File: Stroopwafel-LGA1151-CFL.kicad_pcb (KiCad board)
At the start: 2 copper layers, 1 part

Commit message: rotated socket
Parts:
- turned JCPU1 to 180 degrees
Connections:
- JCPU1 pad AB40: (no net) -> unconnected-(JCPU1B-DDR_VREF_CA-PadAB40)
- JCPU1 pad AC39: (no net) -> unconnected-(JCPU1B-DDR1_VREF_DQ-PadAC39)
- JCPU1 pad AC40: (no net) -> unconnected-(JCPU1B-DDR0_VREF_DQ-PadAC40)
- JCPU1 pad AD34: (no net) -> unconnected-(JCPU1B-DDR1_DQ_0/DDR0_DQ_16-PadAD34)
- JCPU1 pad AD35: (no net) -> unconnected-(JCPU1B-DDR1_DQ_1/DDR0_DQ_17-PadAD35)
- JCPU1 pad AE34: (no net) -> unconnected-(JCPU1B-DDR1_DQ_5/DDR0_DQ_21-PadAE34)
- JCPU1 pad AE35: (no net) -> unconnected-(JCPU1B-DDR1_DQ_4/DDR0_DQ_20-PadAE35)
- JCPU1 pad AE6: (no net) -> unconnected-(JCPU1B-DDR1_DQ_58/DDR1_DQ_58-PadAE6)
- JCPU1 pad AE7: (no net) -> unconnected-(JCPU1B-DDR1_DQ_62/DDR1_DQ_62-PadAE7)
- JCPU1 pad AF34: (no net) -> unconnected-(JCPU1B-DDR1_DQSN_0/DDR0_DQSN_2-PadAF34)
- JCPU1 pad AF35: (no net) -> unconnected-(JCPU1B-DDR1_DQSP_0/DDR0_DQSP_2-PadAF35)
- JCPU1 pad AF38: (no net) -> unconnected-(JCPU1A-DDR0_DQSP_0/DDR0_DQSP_0-PadAF38)
- JCPU1 pad AF39: (no net) -> unconnected-(JCPU1A-DDR0_DQSN_0/DDR0_DQSN_0-PadAF39)
- JCPU1 pad AF6: (no net) -> unconnected-(JCPU1B-DDR1_DQ_63/DDR1_DQ_63-PadAF6)
- JCPU1 pad AF7: (no net) -> unconnected-(JCPU1B-DDR1_DQ_59/DDR1_DQ_59-PadAF7)
- JCPU1 pad AG34: (no net) -> unconnected-(JCPU1B-DDR1_DQ_6/DDR0_DQ_22-PadAG34)
- JCPU1 pad AG35: (no net) -> unconnected-(JCPU1B-DDR1_DQ_2/DDR0_DQ_18-PadAG35)
- JCPU1 pad AG6: (no net) -> unconnected-(JCPU1B-DDR1_DQSN_7/DDR1_DQSN_7-PadAG6)
- JCPU1 pad AG7: (no net) -> unconnected-(JCPU1B-DDR1_DQSP_7/DDR1_DQSP_7-PadAG7)
- JCPU1 pad AH34: (no net) -> unconnected-(JCPU1B-DDR1_DQ_7/DDR0_DQ_23-PadAH34)
- JCPU1 pad AH35: (no net) -> unconnected-(JCPU1B-DDR1_DQ_3/DDR0_DQ_19-PadAH35)
- JCPU1 pad AH6: (no net) -> unconnected-(JCPU1B-DDR1_DQ_61/DDR1_DQ_61-PadAH6)
- JCPU1 pad AH7: (no net) -> unconnected-(JCPU1B-DDR1_DQ_60/DDR1_DQ_60-PadAH7)
- JCPU1 pad AJ2: (no net) -> unconnected-(JCPU1A-DDR0_DQSP_7/DDR1_DQSP_5-PadAJ2)
- JCPU1 pad AJ3: (no net) -> unconnected-(JCPU1A-DDR0_DQSN_7/DDR1_DQSN_5-PadAJ3)
- JCPU1 pad AJ6: (no net) -> unconnected-(JCPU1B-DDR1_DQ_56/DDR1_DQ_56-PadAJ6)
- JCPU1 pad AJ7: (no net) -> unconnected-(JCPU1B-DDR1_DQ_57/DDR1_DQ_57-PadAJ7)
- JCPU1 pad AK31: (no net) -> unconnected-(JCPU1B-DDR1_DQ_14/DDR0_DQ_30-PadAK31)
- JCPU1 pad AK32: (no net) -> unconnected-(JCPU1B-DDR1_DQ_10/DDR0_DQ_26-PadAK32)
- JCPU1 pad AK33: (no net) -> unconnected-(JCPU1B-DDR1_DQSN_1/DDR0_DQSN_3-PadAK33)
- JCPU1 pad AK34: (no net) -> unconnected-(JCPU1B-DDR1_DQ_12/DDR0_DQ_28-PadAK34)
- JCPU1 pad AK35: (no net) -> unconnected-(JCPU1B-DDR1_DQ_8/DDR0_DQ_24-PadAK35)
- JCPU1 pad AK38: (no net) -> unconnected-(JCPU1A-DDR0_DQSP_1/DDR0_DQSP_1-PadAK38)
- JCPU1 pad AK39: (no net) -> unconnected-(JCPU1A-DDR0_DQSN_1/DDR0_DQSN_1-PadAK39)
- JCPU1 pad AL10: (no net) -> unconnected-(JCPU1B-DDR1_DQ_49/DDR1_DQ_49-PadAL10)
- JCPU1 pad AL12: (no net) -> unconnected-(JCPU1B-DDR1_DQ_39/DDR1_DQ_23-PadAL12)
- JCPU1 pad AL13: (no net) -> unconnected-(JCPU1B-DDR1_DQ_35/DDR1_DQ_19-PadAL13)
- JCPU1 pad AL15: (no net) -> unconnected-(JCPU1B-DDR1_ODT_3-PadAL15)
- JCPU1 pad AL16: (no net) -> unconnected-(JCPU1B-DDR1_ODT_1-PadAL16)
- JCPU1 pad AL17: (no net) -> unconnected-(JCPU1B-DDR1_MA_14-PadAL17)
- JCPU1 pad AL18: (no net) -> unconnected-(JCPU1B-DDR1_BA_0-PadAL18)
- JCPU1 pad AL19: (no net) -> unconnected-(JCPU1B-DDR1_MA_0-PadAL19)
- JCPU1 pad AL20: (no net) -> unconnected-(JCPU1B-DDR1_PAR-PadAL20)
- JCPU1 pad AL22: (no net) -> unconnected-(JCPU1B-DDR1_MA_1-PadAL22)
- JCPU1 pad AL23: (no net) -> unconnected-(JCPU1B-DDR1_MA_5-PadAL23)
- JCPU1 pad AL25: (no net) -> unconnected-(JCPU1B-DDR1_ECC_6-PadAL25)
- JCPU1 pad AL26: (no net) -> unconnected-(JCPU1B-DDR1_ECC_7-PadAL26)
- JCPU1 pad AL28: (no net) -> unconnected-(JCPU1B-DDR1_DQ_29/DDR0_DQ_61-PadAL28)
- JCPU1 pad AL29: (no net) -> unconnected-(JCPU1B-DDR1_DQ_24/DDR0_DQ_56-PadAL29)
- JCPU1 pad AL31: (no net) -> unconnected-(JCPU1B-DDR1_DQ_15/DDR0_DQ_31-PadAL31)
- JCPU1 pad AL32: (no net) -> unconnected-(JCPU1B-DDR1_DQ_11/DDR0_DQ_27-PadAL32)
- JCPU1 pad AL33: (no net) -> unconnected-(JCPU1B-DDR1_DQSP_1/DDR0_DQSP_3-PadAL33)
- JCPU1 pad AL34: (no net) -> unconnected-(JCPU1B-DDR1_DQ_13/DDR0_DQ_29-PadAL34)
- JCPU1 pad AL35: (no net) -> unconnected-(JCPU1B-DDR1_DQ_9/DDR0_DQ_25-PadAL35)
- JCPU1 pad AL6: (no net) -> unconnected-(JCPU1B-DDR1_DQ_55/DDR1_DQ_55-PadAL6)
- JCPU1 pad AL7: (no net) -> unconnected-(JCPU1B-DDR1_DQ_51/DDR1_DQ_51-PadAL7)
- JCPU1 pad AL8: (no net) -> unconnected-(JCPU1B-DDR1_DQSP_6/DDR1_DQSP_6-PadAL8)
- JCPU1 pad AL9: (no net) -> unconnected-(JCPU1B-DDR1_DQ_53/DDR1_DQ_53-PadAL9)
- JCPU1 pad AM10: (no net) -> unconnected-(JCPU1B-DDR1_DQ_48/DDR1_DQ_48-PadAM10)
- JCPU1 pad AM12: (no net) -> unconnected-(JCPU1B-DDR1_DQ_38/DDR1_DQ_22-PadAM12)
- JCPU1 pad AM13: (no net) -> unconnected-(JCPU1B-DDR1_DQ_34/DDR1_DQ_18-PadAM13)
- JCPU1 pad AM15: (no net) -> unconnected-(JCPU1B-DDR1_CS#_3-PadAM15)
- JCPU1 pad AM16: (no net) -> unconnected-(JCPU1B-DDR1_ODT_0-PadAM16)
- JCPU1 pad AM18: (no net) -> unconnected-(JCPU1B-DDR1_BA_1-PadAM18)
- JCPU1 pad AM20: (no net) -> unconnected-(JCPU1B-DDR1_CKP_0-PadAM20)
- JCPU1 pad AM21: (no net) -> unconnected-(JCPU1B-DDR1_CKN_0-PadAM21)
- JCPU1 pad AM22: (no net) -> unconnected-(JCPU1B-DDR1_MA_2-PadAM22)
- JCPU1 pad AM23: (no net) -> unconnected-(JCPU1B-DDR1_MA_3-PadAM23)
- JCPU1 pad AM25: (no net) -> unconnected-(JCPU1B-DDR1_ECC_3-PadAM25)
- JCPU1 pad AM26: (no net) -> unconnected-(JCPU1B-DDR1_ECC_2-PadAM26)
- JCPU1 pad AM28: (no net) -> unconnected-(JCPU1B-DDR1_DQ_28/DDR0_DQ_60-PadAM28)
- JCPU1 pad AM29: (no net) -> unconnected-(JCPU1B-DDR1_DQ_25/DDR0_DQ_57-PadAM29)
- JCPU1 pad AM6: (no net) -> unconnected-(JCPU1B-DDR1_DQ_54/DDR1_DQ_54-PadAM6)
- JCPU1 pad AM7: (no net) -> unconnected-(JCPU1B-DDR1_DQ_50/DDR1_DQ_50-PadAM7)
- JCPU1 pad AM8: (no net) -> unconnected-(JCPU1B-DDR1_DQSN_6/DDR1_DQSN_6-PadAM8)
- JCPU1 pad AM9: (no net) -> unconnected-(JCPU1B-DDR1_DQ_52/DDR1_DQ_52-PadAM9)
- JCPU1 pad AN12: (no net) -> unconnected-(JCPU1B-DDR1_DQSP_4/DDR1_DQSP_2-PadAN12)
- JCPU1 pad AN13: (no net) -> unconnected-(JCPU1B-DDR1_DQSN_4/DDR1_DQSN_2-PadAN13)
- JCPU1 pad AN15: (no net) -> unconnected-(JCPU1B-DDR1_CS#_1-PadAN15)
- JCPU1 pad AN17: (no net) -> unconnected-(JCPU1B-DDR1_CS#_2-PadAN17)
- JCPU1 pad AN18: (no net) -> unconnected-(JCPU1B-DDR1_MA_16-PadAN18)
- JCPU1 pad AN2: (no net) -> unconnected-(JCPU1A-DDR0_DQSP_6/DDR1_DQSP_4-PadAN2)
- JCPU1 pad AN20: (no net) -> unconnected-(JCPU1B-DDR1_CKP_2-PadAN20)
- JCPU1 pad AN21: (no net) -> unconnected-(JCPU1B-DDR1_CKN_2-PadAN21)
- JCPU1 pad AN25: (no net) -> unconnected-(JCPU1B-DDR1_DQSP_8/DDR1_DQSP_8-PadAN25)
- JCPU1 pad AN26: (no net) -> unconnected-(JCPU1B-DDR1_DQSN_8/DDR1_DQSN_8-PadAN26)
- JCPU1 pad AN28: (no net) -> unconnected-(JCPU1B-DDR1_DQSP_3/DDR0_DQSP_7-PadAN28)
- JCPU1 pad AN29: (no net) -> unconnected-(JCPU1B-DDR1_DQSN_3/DDR0_DQSN_7-PadAN29)
- JCPU1 pad AN3: (no net) -> unconnected-(JCPU1A-DDR0_DQSN_6/DDR1_DQSN_4-PadAN3)
- JCPU1 pad AN31: (no net) -> unconnected-(JCPU1B-DDR1_DQ_22/DDR0_DQ_54-PadAN31)
- JCPU1 pad AN32: (no net) -> unconnected-(JCPU1B-DDR1_DQ_18/DDR0_DQ_50-PadAN32)
- JCPU1 pad AN33: (no net) -> unconnected-(JCPU1B-DDR1_DQSN_2/DDR0_DQSN_6-PadAN33)
- JCPU1 pad AN34: (no net) -> unconnected-(JCPU1B-DDR1_DQ_20/DDR0_DQ_52-PadAN34)
- JCPU1 pad AN35: (no net) -> unconnected-(JCPU1B-DDR1_DQ_17/DDR0_DQ_49-PadAN35)
- JCPU1 pad AP10: (no net) -> unconnected-(JCPU1B-DDR1_DQ_40/DDR1_DQ_24-PadAP10)
- JCPU1 pad AP12: (no net) -> unconnected-(JCPU1B-DDR1_DQ_33/DDR1_DQ_17-PadAP12)
- JCPU1 pad AP13: (no net) -> unconnected-(JCPU1B-DDR1_DQ_37/DDR1_DQ_21-PadAP13)
- JCPU1 pad AP15: (no net) -> unconnected-(JCPU1B-DDR1_ODT_2-PadAP15)
- JCPU1 pad AP16: (no net) -> unconnected-(JCPU1B-DDR1_MA_15-PadAP16)
- JCPU1 pad AP17: (no net) -> unconnected-(JCPU1B-DDR1_CS#_0-PadAP17)
- JCPU1 pad AP18: (no net) -> unconnected-(JCPU1B-DDR1_MA_10-PadAP18)
- JCPU1 pad AP19: (no net) -> unconnected-(JCPU1B-DDR1_CKP_3-PadAP19)
- JCPU1 pad AP20: (no net) -> unconnected-(JCPU1B-DDR1_CKN_3-PadAP20)
- JCPU1 pad AP21: (no net) -> unconnected-(JCPU1B-DDR1_CKN_1-PadAP21)
- JCPU1 pad AP22: (no net) -> unconnected-(JCPU1B-DDR1_CKP_1-PadAP22)
- JCPU1 pad AP23: (no net) -> unconnected-(JCPU1B-DDR1_MA_4-PadAP23)
- JCPU1 pad AP25: (no net) -> unconnected-(JCPU1B-DDR1_ECC_5-PadAP25)
- JCPU1 pad AP26: (no net) -> unconnected-(JCPU1B-DDR1_ECC_4-PadAP26)
- JCPU1 pad AP28: (no net) -> unconnected-(JCPU1B-DDR1_DQ_31/DDR0_DQ_63-PadAP28)
- JCPU1 pad AP29: (no net) -> unconnected-(JCPU1B-DDR1_DQ_26/DDR0_DQ_58-PadAP29)
- JCPU1 pad AP31: (no net) -> unconnected-(JCPU1B-DDR1_DQ_23/DDR0_DQ_55-PadAP31)
- JCPU1 pad AP32: (no net) -> unconnected-(JCPU1B-DDR1_DQ_19/DDR0_DQ_51-PadAP32)
- JCPU1 pad AP33: (no net) -> unconnected-(JCPU1B-DDR1_DQSP_2/DDR0_DQSP_6-PadAP33)
- JCPU1 pad AP34: (no net) -> unconnected-(JCPU1B-DDR1_DQ_21/DDR0_DQ_53-PadAP34)
- JCPU1 pad AP35: (no net) -> unconnected-(JCPU1B-DDR1_DQ_16/DDR0_DQ_48-PadAP35)
- JCPU1 pad AP38: (no net) -> unconnected-(JCPU1A-DDR0_DQSP_2/DDR0_DQSP_4-PadAP38)
- JCPU1 pad AP39: (no net) -> unconnected-(JCPU1A-DDR0_DQSN_2/DDR0_DQSN_4-PadAP39)
- JCPU1 pad AP6: (no net) -> unconnected-(JCPU1B-DDR1_DQ_47/DDR1_DQ_31-PadAP6)
- JCPU1 pad AP7: (no net) -> unconnected-(JCPU1B-DDR1_DQ_43/DDR1_DQ_27-PadAP7)
- JCPU1 pad AP8: (no net) -> unconnected-(JCPU1B-DDR1_DQSP_5/DDR1_DQSP_3-PadAP8)
- JCPU1 pad AP9: (no net) -> unconnected-(JCPU1B-DDR1_DQ_45/DDR1_DQ_29-PadAP9)
- JCPU1 pad AR10: (no net) -> unconnected-(JCPU1B-DDR1_DQ_41/DDR1_DQ_25-PadAR10)
- JCPU1 pad AR12: (no net) -> unconnected-(JCPU1B-DDR1_DQ_32/DDR1_DQ_16-PadAR12)
- JCPU1 pad AR13: (no net) -> unconnected-(JCPU1B-DDR1_DQ_36/DDR1_DQ_20-PadAR13)
- JCPU1 pad AR15: (no net) -> unconnected-(JCPU1B-DDR1_MA_13-PadAR15)
- JCPU1 pad AR25: (no net) -> unconnected-(JCPU1B-DDR1_ECC_0-PadAR25)
- JCPU1 pad AR26: (no net) -> unconnected-(JCPU1B-DDR1_ECC_1-PadAR26)
- JCPU1 pad AR28: (no net) -> unconnected-(JCPU1B-DDR1_DQ_30/DDR0_DQ_62-PadAR28)
- JCPU1 pad AR29: (no net) -> unconnected-(JCPU1B-DDR1_DQ_27/DDR0_DQ_59-PadAR29)
- JCPU1 pad AR6: (no net) -> unconnected-(JCPU1B-DDR1_DQ_46/DDR1_DQ_30-PadAR6)
- JCPU1 pad AR7: (no net) -> unconnected-(JCPU1B-DDR1_DQ_42/DDR1_DQ_26-PadAR7)
- JCPU1 pad AR8: (no net) -> unconnected-(JCPU1B-DDR1_DQSN_5/DDR1_DQSN_3-PadAR8)
- JCPU1 pad AR9: (no net) -> unconnected-(JCPU1B-DDR1_DQ_44/DDR1_DQ_28-PadAR9)
- JCPU1 pad AT16: (no net) -> unconnected-(JCPU1A-DDR0_CKP_3-PadAT16)
- JCPU1 pad AT19: (no net) -> unconnected-(JCPU1A-DDR0_MA_4-PadAT19)
- JCPU1 pad AT20: (no net) -> unconnected-(JCPU1A-DDR0_MA_8-PadAT20)
- JCPU1 pad AT22: (no net) -> unconnected-(JCPU1A-DDR0_MA_9-PadAT22)
- JCPU1 pad AT23: (no net) -> unconnected-(JCPU1A-DDR0_ALERT#-PadAT23)
- JCPU1 pad AU11: (no net) -> unconnected-(JCPU1A-DDR0_CS#_1-PadAU11)
- JCPU1 pad AU12: (no net) -> unconnected-(JCPU1A-DDR0_ODT_2-PadAU12)
- JCPU1 pad AU14: (no net) -> unconnected-(JCPU1A-DDR0_ODT_1-PadAU14)
- JCPU1 pad AU16: (no net) -> unconnected-(JCPU1A-DDR0_CKN_3-PadAU16)
- JCPU1 pad AU17: (no net) -> unconnected-(JCPU1A-DDR0_MA_2-PadAU17)
- JCPU1 pad AU18: (no net) -> unconnected-(JCPU1A-DDR0_MA_1-PadAU18)
- JCPU1 pad AU2: (no net) -> unconnected-(JCPU1A-DDR0_DQSP_5/DDR1_DQSP_1-PadAU2)
- JCPU1 pad AU20: (no net) -> unconnected-(JCPU1A-DDR0_MA_5-PadAU20)
- JCPU1 pad AU21: (no net) -> unconnected-(JCPU1A-DDR0_MA_7-PadAU21)
- JCPU1 pad AU22: (no net) -> unconnected-(JCPU1A-DDR0_MA_11-PadAU22)
- JCPU1 pad AU24: (no net) -> unconnected-(JCPU1A-DDR0_ACT#-PadAU24)
- JCPU1 pad AU26: (no net) -> unconnected-(JCPU1B-DDR1_MA_8-PadAU26)
- JCPU1 pad AU27: (no net) -> unconnected-(JCPU1B-DDR1_MA_11-PadAU27)
- JCPU1 pad AU28: (no net) -> unconnected-(JCPU1B-DDR1_ACT#-PadAU28)
- JCPU1 pad AU29: (no net) -> unconnected-(JCPU1B-DDR1_CKE_3-PadAU29)
- JCPU1 pad AU3: (no net) -> unconnected-(JCPU1A-DDR0_DQSN_5/DDR1_DQSN_1-PadAU3)
- JCPU1 pad AU32: (no net) -> unconnected-(JCPU1A-DDR0_DQSN_8/DDR0_DQSN_8-PadAU32)
- JCPU1 pad AU36: (no net) -> unconnected-(JCPU1A-DDR0_DQSN_3/DDR0_DQSN_5-PadAU36)
- JCPU1 pad AV10: (no net) -> unconnected-(JCPU1A-DDR0_CS#_3-PadAV10)
- JCPU1 pad AV12: (no net) -> unconnected-(JCPU1A-DDR0_MA_13-PadAV12)
- JCPU1 pad AV13: (no net) -> unconnected-(JCPU1A-DDR0_CS#_2-PadAV13)
- JCPU1 pad AV14: (no net) -> unconnected-(JCPU1A-DDR0_MA_14-PadAV14)
- JCPU1 pad AV15: (no net) -> unconnected-(JCPU1A-DDR0_BA_1-PadAV15)
- JCPU1 pad AV16: (no net) -> unconnected-(JCPU1A-DDR0_CKN_2-PadAV16)
- JCPU1 pad AV18: (no net) -> unconnected-(JCPU1A-DDR0_CKN_0-PadAV18)
- JCPU1 pad AV19: (no net) -> unconnected-(JCPU1A-DDR0_MA_3-PadAV19)
- JCPU1 pad AV20: (no net) -> unconnected-(JCPU1A-DDR0_MA_6-PadAV20)
- JCPU1 pad AV22: (no net) -> unconnected-(JCPU1A-DDR0_MA_12-PadAV22)
- JCPU1 pad AV23: (no net) -> unconnected-(JCPU1A-DDR0_BG_1-PadAV23)
- JCPU1 pad AV24: (no net) -> unconnected-(JCPU1A-DDR0_CKE_2-PadAV24)
- JCPU1 pad AV25: (no net) -> unconnected-(JCPU1A-DDR0_CKE_3-PadAV25)
- JCPU1 pad AV27: (no net) -> unconnected-(JCPU1B-DDR1_MA_12-PadAV27)
- JCPU1 pad AV29: (no net) -> unconnected-(JCPU1B-DDR1_CKE_1-PadAV29)
- JCPU1 pad AV32: (no net) -> unconnected-(JCPU1A-DDR0_DQSP_8/DDR0_DQSP_8-PadAV32)
- JCPU1 pad AV36: (no net) -> unconnected-(JCPU1A-DDR0_DQSP_3/DDR0_DQSP_5-PadAV36)
- JCPU1 pad AV7: (no net) -> unconnected-(JCPU1A-DDR0_DQSP_4/DDR1_DQSP_0-PadAV7)
- JCPU1 pad AW11: (no net) -> unconnected-(JCPU1A-DDR0_ODT_0-PadAW11)
- JCPU1 pad AW12: (no net) -> unconnected-(JCPU1A-DDR0_CS#_0-PadAW12)
- JCPU1 pad AW13: (no net) -> unconnected-(JCPU1A-DDR0_MA_16-PadAW13)
- JCPU1 pad AW15: (no net) -> unconnected-(JCPU1A-DDR0_MA_0-PadAW15)
- JCPU1 pad AW16: (no net) -> unconnected-(JCPU1A-DDR0_CKP_2-PadAW16)
- JCPU1 pad AW17: (no net) -> unconnected-(JCPU1A-DDR0_CKP_1-PadAW17)
- JCPU1 pad AW18: (no net) -> unconnected-(JCPU1A-DDR0_CKP_0-PadAW18)
- JCPU1 pad AW23: (no net) -> unconnected-(JCPU1A-DDR0_BG_0-PadAW23)
- JCPU1 pad AW24: (no net) -> unconnected-(JCPU1A-DDR0_CKE_1-PadAW24)
- JCPU1 pad AW26: (no net) -> unconnected-(JCPU1B-DDR1_MA_6-PadAW26)
- JCPU1 pad AW27: (no net) -> unconnected-(JCPU1B-DDR1_MA_9-PadAW27)
- JCPU1 pad AW28: (no net) -> unconnected-(JCPU1B-DDR1_BG_0-PadAW28)
- JCPU1 pad AW29: (no net) -> unconnected-(JCPU1B-DDR1_CKE_2-PadAW29)
- JCPU1 pad AW7: (no net) -> unconnected-(JCPU1A-DDR0_DQSN_4/DDR1_DQSN_0-PadAW7)
- JCPU1 pad AY10: (no net) -> unconnected-(JCPU1A-DDR0_ODT_3-PadAY10)
- JCPU1 pad AY11: (no net) -> unconnected-(JCPU1A-DDR0_MA_15-PadAY11)
- JCPU1 pad AY13: (no net) -> unconnected-(JCPU1A-DDR0_BA_0-PadAY13)
- JCPU1 pad AY14: (no net) -> unconnected-(JCPU1A-DDR0_MA_10-PadAY14)
- JCPU1 pad AY15: (no net) -> unconnected-(JCPU1A-DDR0_PAR-PadAY15)
- JCPU1 pad AY17: (no net) -> unconnected-(JCPU1A-DDR0_CKN_1-PadAY17)
- JCPU1 pad AY24: (no net) -> unconnected-(JCPU1A-DDR0_CKE_0-PadAY24)
- JCPU1 pad AY25: (no net) -> unconnected-(JCPU1B-DDR1_ALERT#-PadAY25)
- JCPU1 pad AY26: (no net) -> unconnected-(JCPU1B-DDR1_MA_7-PadAY26)
- JCPU1 pad AY28: (no net) -> unconnected-(JCPU1B-DDR1_BG_1-PadAY28)
- JCPU1 pad AY29: (no net) -> unconnected-(JCPU1B-DDR1_CKE_0-PadAY29)

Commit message: Connected CPU ground
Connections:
- JCPU1 pad A11: (no net) -> GND
- JCPU1 pad A12: (no net) -> unconnected-(JCPU1D-DDI2_AUXP-PadA12)
- JCPU1 pad A13: (no net) -> GND
- JCPU1 pad A14: (no net) -> unconnected-(JCPU1D-DDI3_TXN_0-PadA14)
- JCPU1 pad A15: (no net) -> GND
- JCPU1 pad A16: (no net) -> unconnected-(JCPU1D-DDI3_TXN_2-PadA16)
- JCPU1 pad A17: (no net) -> GND
- JCPU1 pad A18: (no net) -> unconnected-(JCPU1D-DDI2_TXN_0-PadA18)
- JCPU1 pad A23: (no net) -> unconnected-(JCPU1D-DDI1_TXN_2-PadA23)
- JCPU1 pad A24: (no net) -> GND
- JCPU1 pad A25: (no net) -> unconnected-(JCPU1G-VCC_CORE-PadA25)
- JCPU1 pad A26: (no net) -> unconnected-(JCPU1G-VCC_CORE-PadA26)
- JCPU1 pad A27: (no net) -> unconnected-(JCPU1G-VCC_CORE-PadA27)
- JCPU1 pad A28: (no net) -> unconnected-(JCPU1G-VCC_CORE-PadA28)
- JCPU1 pad A29: (no net) -> unconnected-(JCPU1G-VCC_CORE-PadA29)
- JCPU1 pad A30: (no net) -> unconnected-(JCPU1G-VCC_CORE-PadA30)
- JCPU1 pad A4: (no net) -> GND
- JCPU1 pad A5: (no net) -> unconnected-(JCPU1C-PEG_TXP_0-PadA5)
- JCPU1 pad A6: (no net) -> unconnected-(JCPU1C-PEG_TXN_0-PadA6)
- JCPU1 pad A7: (no net) -> GND
- JCPU1 pad AA3: (no net) -> GND
- JCPU1 pad AA33: (no net) -> GND
- JCPU1 pad AA34: (no net) -> unconnected-(JCPU1H-VCCGT-PadAA34)
- JCPU1 pad AA35: (no net) -> unconnected-(JCPU1H-VCCGT-PadAA35)
- JCPU1 pad AA36: (no net) -> unconnected-(JCPU1H-VCCGT-PadAA36)
- JCPU1 pad AA37: (no net) -> unconnected-(JCPU1H-VCCGT-PadAA37)
- JCPU1 pad AA38: (no net) -> unconnected-(JCPU1H-VCCGT-PadAA38)
- JCPU1 pad AA4: (no net) -> unconnected-(JCPU1C-DMI_RXP_1-PadAA4)
- JCPU1 pad AA5: (no net) -> unconnected-(JCPU1C-DMI_RXN_1-PadAA5)
- JCPU1 pad AA6: (no net) -> unconnected-(JCPU1I-VCCSA-PadAA6)
- JCPU1 pad AA7: (no net) -> unconnected-(JCPU1I-VCCSA-PadAA7)
- JCPU1 pad AA8: (no net) -> GND
- JCPU1 pad AB3: (no net) -> unconnected-(JCPU1C-DMI_RXN_2-PadAB3)
- JCPU1 pad AB33: (no net) -> unconnected-(JCPU1H-VCCGT-PadAB33)
- JCPU1 pad AB34: (no net) -> unconnected-(JCPU1H-VCCGT-PadAB34)
- JCPU1 pad AB35: (no net) -> unconnected-(JCPU1J-RSVD1-PadAB35)
- JCPU1 pad AB36: (no net) -> unconnected-(JCPU1E-PROC_SELECT#-PadAB36)
- JCPU1 pad AB37: (no net) -> unconnected-(JCPU1J-RSVD2-PadAB37)
- JCPU1 pad AB38: (no net) -> unconnected-(JCPU1J-RSVD3-PadAB38)
- JCPU1 pad AB39: (no net) -> GND
- JCPU1 pad AB4: (no net) -> unconnected-(JCPU1C-DMI_RXP_2-PadAB4)
- JCPU1 pad AB5: (no net) -> GND
- JCPU1 pad AB6: (no net) -> unconnected-(JCPU1I-VCCSA-PadAB6)
- JCPU1 pad AB7: (no net) -> unconnected-(JCPU1I-VCCSA-PadAB7)
- JCPU1 pad AB8: (no net) -> unconnected-(JCPU1I-VCCSA-PadAB8)
- JCPU1 pad AC1: (no net) -> unconnected-(JCPU1C-DMI_TXN_0-PadAC1)
- JCPU1 pad AC2: (no net) -> unconnected-(JCPU1C-DMI_TXP_0-PadAC2)
- JCPU1 pad AC3: (no net) -> GND
- JCPU1 pad AC33: (no net) -> GND
- JCPU1 pad AC34: (no net) -> GND
- JCPU1 pad AC35: (no net) -> GND
- JCPU1 pad AC36: (no net) -> unconnected-(JCPU1E-DDR_VTT_CNTL-PadAC36)
- JCPU1 pad AC37: (no net) -> unconnected-(JCPU1J-RSVD4-PadAC37)
- JCPU1 pad AC38: (no net) -> unconnected-(JCPU1E-SKTOCC#-PadAC38)
- JCPU1 pad AC4: (no net) -> unconnected-(JCPU1C-DMI_RXP_3-PadAC4)
- JCPU1 pad AC5: (no net) -> unconnected-(JCPU1C-DMI_RXN_3-PadAC5)
- JCPU1 pad AC6: (no net) -> GND
- JCPU1 pad AC7: (no net) -> unconnected-(JCPU1I-VCCSA-PadAC7)
- JCPU1 pad AC8: (no net) -> unconnected-(JCPU1I-VCCSA-PadAC8)
- JCPU1 pad AD1: (no net) -> GND
- JCPU1 pad AD2: (no net) -> unconnected-(JCPU1C-DMI_TXN_1-PadAD2)
- JCPU1 pad AD3: (no net) -> unconnected-(JCPU1C-DMI_TXP_1-PadAD3)
- JCPU1 pad AD33: (no net) -> GND
- JCPU1 pad AD36: (no net) -> GND
- JCPU1 pad AD37: (no net) -> GND
- JCPU1 pad AD38: (no net) -> GND
- JCPU1 pad AD39: (no net) -> GND
- JCPU1 pad AD4: (no net) -> GND
- JCPU1 pad AD40: (no net) -> GND
- JCPU1 pad AD5: (no net) -> unconnected-(JCPU1I-VCCSA_SENSE-PadAD5)
- JCPU1 pad AD6: (no net) -> GND
- JCPU1 pad AD7: (no net) -> GND
- JCPU1 pad AD8: (no net) -> GND
- JCPU1 pad AE1: (no net) -> unconnected-(JCPU1C-DMI_TXN_2-PadAE1)
- JCPU1 pad AE2: (no net) -> unconnected-(JCPU1C-DMI_TXP_2-PadAE2)
- JCPU1 pad AE3: (no net) -> GND
- JCPU1 pad AE33: (no net) -> GND
- JCPU1 pad AE36: (no net) -> GND
- JCPU1 pad AE4: (no net) -> unconnected-(JCPU1I-VSS_SAIO_SENSE-PadAE4)
- JCPU1 pad AE5: (no net) -> GND
- JCPU1 pad AE8: (no net) -> GND
- JCPU1 pad AF1: (no net) -> GND
- JCPU1 pad AF2: (no net) -> unconnected-(JCPU1C-DMI_TXP_3-PadAF2)
- JCPU1 pad AF3: (no net) -> unconnected-(JCPU1C-DMI_TXN_3-PadAF3)
- JCPU1 pad AF33: (no net) -> GND
- JCPU1 pad AF36: (no net) -> GND
- JCPU1 pad AF37: (no net) -> GND
- JCPU1 pad AF4: (no net) -> unconnected-(JCPU1I-VCCIO_SENSE-PadAF4)
- JCPU1 pad AF40: (no net) -> GND
- JCPU1 pad AF5: (no net) -> GND
- JCPU1 pad AF8: (no net) -> GND
- JCPU1 pad AG1: (no net) -> GND
- JCPU1 pad AG2: (no net) -> GND
- JCPU1 pad AG3: (no net) -> GND
- JCPU1 pad AG33: (no net) -> GND
- JCPU1 pad AG36: (no net) -> GND
- JCPU1 pad AG4: (no net) -> GND
- JCPU1 pad AG5: (no net) -> GND
- JCPU1 pad AG8: (no net) -> GND
- JCPU1 pad AH33: (no net) -> GND
- JCPU1 pad AH36: (no net) -> GND
- JCPU1 pad AH37: (no net) -> GND
- JCPU1 pad AH38: (no net) -> GND
- JCPU1 pad AH39: (no net) -> GND
- JCPU1 pad AH40: (no net) -> GND
- JCPU1 pad AH5: (no net) -> GND
- JCPU1 pad AH8: (no net) -> GND
- JCPU1 pad AJ1: (no net) -> GND
- JCPU1 pad AJ11: (no net) -> unconnected-(JCPU1G-VCC_CORE-PadAJ11)
- JCPU1 pad AJ12: (no net) -> unconnected-(JCPU1G-VCC_CORE-PadAJ12)
- JCPU1 pad AJ13: (no net) -> unconnected-(JCPU1G-VCC_CORE-PadAJ13)
- JCPU1 pad AJ14: (no net) -> unconnected-(JCPU1G-VCC_CORE-PadAJ14)
- JCPU1 pad AJ15: (no net) -> unconnected-(JCPU1G-VCC_CORE-PadAJ15)
- JCPU1 pad AJ16: (no net) -> unconnected-(JCPU1G-VCC_CORE-PadAJ16)
- JCPU1 pad AJ17: (no net) -> unconnected-(JCPU1G-VCC_CORE-PadAJ17)
- JCPU1 pad AJ18: (no net) -> unconnected-(JCPU1G-VCC_CORE-PadAJ18)
- JCPU1 pad AJ19: (no net) -> unconnected-(JCPU1G-VCC_CORE-PadAJ19)
- JCPU1 pad AJ20: (no net) -> unconnected-(JCPU1G-VCC_CORE-PadAJ20)
- JCPU1 pad AJ21: (no net) -> unconnected-(JCPU1G-VCC_CORE-PadAJ21)
- JCPU1 pad AJ22: (no net) -> unconnected-(JCPU1J-RSVD5-PadAJ22)
- JCPU1 pad AJ23: (no net) -> unconnected-(JCPU1I-VCCIO-PadAJ23)
- JCPU1 pad AJ24: (no net) -> GND
- JCPU1 pad AJ25: (no net) -> unconnected-(JCPU1G-VCC_CORE-PadAJ25)
- JCPU1 pad AJ26: (no net) -> unconnected-(JCPU1G-VCC_CORE-PadAJ26)
- JCPU1 pad AJ27: (no net) -> unconnected-(JCPU1G-VCC_CORE-PadAJ27)
- JCPU1 pad AJ28: (no net) -> unconnected-(JCPU1G-VCC_CORE-PadAJ28)
- JCPU1 pad AJ29: (no net) -> unconnected-(JCPU1G-VCC_CORE-PadAJ29)
- JCPU1 pad AJ30: (no net) -> GND
- JCPU1 pad AJ31: (no net) -> GND
- JCPU1 pad AJ32: (no net) -> GND
- JCPU1 pad AJ33: (no net) -> GND
- JCPU1 pad AJ34: (no net) -> GND
- JCPU1 pad AJ35: (no net) -> GND
- JCPU1 pad AJ36: (no net) -> GND
- JCPU1 pad AJ4: (no net) -> GND
- JCPU1 pad AJ5: (no net) -> GND
- JCPU1 pad AJ8: (no net) -> GND
- JCPU1 pad AJ9: (no net) -> unconnected-(JCPU1I-VCCPLL_OC-PadAJ9)
- JCPU1 pad AK10: (no net) -> GND
- JCPU1 pad AK11: (no net) -> unconnected-(JCPU1I-VCCIO-PadAK11)
- JCPU1 pad AK12: (no net) -> GND
- JCPU1 pad AK13: (no net) -> GND
- JCPU1 pad AK14: (no net) -> unconnected-(JCPU1I-VCCIO-PadAK14)
- JCPU1 pad AK15: (no net) -> GND
- JCPU1 pad AK16: (no net) -> GND
- JCPU1 pad AK17: (no net) -> GND
- JCPU1 pad AK18: (no net) -> GND
- JCPU1 pad AK19: (no net) -> GND
- JCPU1 pad AK20: (no net) -> GND
- JCPU1 pad AK21: (no net) -> unconnected-(JCPU1G-VCC_CORE-PadAK21)
- JCPU1 pad AK22: (no net) -> GND
- JCPU1 pad AK23: (no net) -> GND
- JCPU1 pad AK24: (no net) -> unconnected-(JCPU1I-VCCIO-PadAK24)
- JCPU1 pad AK25: (no net) -> GND
- JCPU1 pad AK26: (no net) -> GND
- JCPU1 pad AK27: (no net) -> GND
- JCPU1 pad AK28: (no net) -> GND
- JCPU1 pad AK29: (no net) -> GND
- JCPU1 pad AK30: (no net) -> GND
- JCPU1 pad AK36: (no net) -> GND
- JCPU1 pad AK37: (no net) -> GND
- JCPU1 pad AK40: (no net) -> GND
- JCPU1 pad AK5: (no net) -> GND
- JCPU1 pad AK6: (no net) -> GND
- JCPU1 pad AK7: (no net) -> GND
- JCPU1 pad AK8: (no net) -> GND
- JCPU1 pad AK9: (no net) -> GND
- JCPU1 pad AL1: (no net) -> GND
- JCPU1 pad AL11: (no net) -> GND
- JCPU1 pad AL14: (no net) -> GND
- JCPU1 pad AL2: (no net) -> GND
- JCPU1 pad AL21: (no net) -> GND
- JCPU1 pad AL24: (no net) -> GND
- JCPU1 pad AL27: (no net) -> GND
- JCPU1 pad AL3: (no net) -> GND
- JCPU1 pad AL30: (no net) -> GND
- JCPU1 pad AL36: (no net) -> GND
- JCPU1 pad AL4: (no net) -> GND
- JCPU1 pad AL5: (no net) -> GND
- JCPU1 pad AM11: (no net) -> GND
- JCPU1 pad AM14: (no net) -> GND
- JCPU1 pad AM17: (no net) -> GND
- JCPU1 pad AM19: (no net) -> GND
- JCPU1 pad AM24: (no net) -> GND
- JCPU1 pad AM27: (no net) -> GND
- JCPU1 pad AM30: (no net) -> GND
- JCPU1 pad AM31: (no net) -> GND
- JCPU1 pad AM32: (no net) -> GND
- JCPU1 pad AM33: (no net) -> GND
- JCPU1 pad AM34: (no net) -> GND
- JCPU1 pad AM35: (no net) -> GND
- JCPU1 pad AM36: (no net) -> GND
- JCPU1 pad AM37: (no net) -> GND
- JCPU1 pad AM38: (no net) -> GND
- JCPU1 pad AM39: (no net) -> GND
- JCPU1 pad AM40: (no net) -> GND
- JCPU1 pad AM5: (no net) -> GND
- JCPU1 pad AN1: (no net) -> GND
- JCPU1 pad AN10: (no net) -> GND
- JCPU1 pad AN11: (no net) -> GND
- JCPU1 pad AN14: (no net) -> GND
- JCPU1 pad AN16: (no net) -> GND
- JCPU1 pad AN19: (no net) -> GND
- JCPU1 pad AN22: (no net) -> GND
- JCPU1 pad AN23: (no net) -> GND
- JCPU1 pad AN24: (no net) -> GND
- JCPU1 pad AN27: (no net) -> GND
- JCPU1 pad AN30: (no net) -> GND
- JCPU1 pad AN36: (no net) -> GND
- JCPU1 pad AN4: (no net) -> GND
- JCPU1 pad AN5: (no net) -> GND
- JCPU1 pad AN6: (no net) -> GND
- JCPU1 pad AN7: (no net) -> GND
- JCPU1 pad AN8: (no net) -> GND
- JCPU1 pad AN9: (no net) -> GND
- JCPU1 pad AP11: (no net) -> GND
- JCPU1 pad AP14: (no net) -> GND
- JCPU1 pad AP24: (no net) -> GND
- JCPU1 pad AP27: (no net) -> GND
- JCPU1 pad AP30: (no net) -> GND
- JCPU1 pad AP36: (no net) -> GND
- JCPU1 pad AP37: (no net) -> GND
- JCPU1 pad AP40: (no net) -> GND
- JCPU1 pad AP5: (no net) -> GND
- JCPU1 pad AR1: (no net) -> GND
- JCPU1 pad AR11: (no net) -> GND
- JCPU1 pad AR14: (no net) -> GND
- JCPU1 pad AR16: (no net) -> GND
- JCPU1 pad AR17: (no net) -> GND
- JCPU1 pad AR18: (no net) -> GND
- JCPU1 pad AR19: (no net) -> GND
- JCPU1 pad AR2: (no net) -> GND
- JCPU1 pad AR20: (no net) -> GND
- JCPU1 pad AR21: (no net) -> GND
- JCPU1 pad AR22: (no net) -> GND
- JCPU1 pad AR23: (no net) -> GND
- JCPU1 pad AR24: (no net) -> GND
- JCPU1 pad AR27: (no net) -> GND
- JCPU1 pad AR3: (no net) -> GND
- JCPU1 pad AR30: (no net) -> GND
- JCPU1 pad AR31: (no net) -> GND
- JCPU1 pad AR32: (no net) -> GND
- JCPU1 pad AR33: (no net) -> GND
- JCPU1 pad AR34: (no net) -> GND
- JCPU1 pad AR35: (no net) -> GND
- JCPU1 pad AR36: (no net) -> GND
- JCPU1 pad AR4: (no net) -> GND
- JCPU1 pad AR5: (no net) -> GND
- JCPU1 pad AT10: (no net) -> GND
- JCPU1 pad AT11: (no net) -> GND
- JCPU1 pad AT12: (no net) -> GND
- JCPU1 pad AT13: (no net) -> GND
- JCPU1 pad AT14: (no net) -> GND
- JCPU1 pad AT15: (no net) -> GND
- JCPU1 pad AT17: (no net) -> GND
- JCPU1 pad AT18: (no net) -> unconnected-(JCPU1I-VDDQ-PadAT18)
- JCPU1 pad AT21: (no net) -> unconnected-(JCPU1I-VDDQ-PadAT21)
- JCPU1 pad AT24: (no net) -> GND
- JCPU1 pad AT25: (no net) -> GND
- JCPU1 pad AT26: (no net) -> GND
- JCPU1 pad AT27: (no net) -> GND
- JCPU1 pad AT28: (no net) -> GND
- JCPU1 pad AT29: (no net) -> GND
- JCPU1 pad AT30: (no net) -> GND
- JCPU1 pad AT31: (no net) -> GND
- JCPU1 pad AT32: (no net) -> GND
- JCPU1 pad AT34: (no net) -> GND
- JCPU1 pad AT36: (no net) -> GND
- JCPU1 pad AT37: (no net) -> GND
- JCPU1 pad AT38: (no net) -> GND
- JCPU1 pad AT39: (no net) -> GND
- JCPU1 pad AT40: (no net) -> GND
- JCPU1 pad AT5: (no net) -> GND
- JCPU1 pad AT6: (no net) -> GND
- JCPU1 pad AT7: (no net) -> GND
- JCPU1 pad AT8: (no net) -> GND
- JCPU1 pad AT9: (no net) -> GND
- JCPU1 pad AU1: (no net) -> GND
- JCPU1 pad AU10: (no net) -> unconnected-(JCPU1J-RSVD6-PadAU10)
- JCPU1 pad AU13: (no net) -> unconnected-(JCPU1I-VDDQ-PadAU13)
- JCPU1 pad AU15: (no net) -> unconnected-(JCPU1I-VDDQ-PadAU15)
- JCPU1 pad AU19: (no net) -> unconnected-(JCPU1I-VDDQ-PadAU19)
- JCPU1 pad AU23: (no net) -> unconnected-(JCPU1I-VDDQ-PadAU23)
- JCPU1 pad AU25: (no net) -> GND
- JCPU1 pad AU30: (no net) -> GND
- JCPU1 pad AU34: (no net) -> GND
- JCPU1 pad AU39: (no net) -> GND
- JCPU1 pad AU4: (no net) -> GND
- JCPU1 pad AU40: (no net) -> GND
- JCPU1 pad AU5: (no net) -> GND
- JCPU1 pad AU7: (no net) -> GND
- JCPU1 pad AU9: (no net) -> unconnected-(JCPU1J-RSVD7-PadAU9)
- JCPU1 pad AV1: (no net) -> unconnected-(JCPU1J-RSVD8-PadAV1)
- JCPU1 pad AV11: (no net) -> unconnected-(JCPU1I-VDDQ-PadAV11)
- JCPU1 pad AV17: (no net) -> unconnected-(JCPU1I-VDDQ-PadAV17)
- JCPU1 pad AV2: (no net) -> GND
- JCPU1 pad AV21: (no net) -> unconnected-(JCPU1I-VDDQ-PadAV21)
- JCPU1 pad AV26: (no net) -> GND
- JCPU1 pad AV28: (no net) -> GND
- JCPU1 pad AV30: (no net) -> GND
- JCPU1 pad AV34: (no net) -> GND
- JCPU1 pad AV38: (no net) -> GND
- JCPU1 pad AV39: (no net) -> GND
- JCPU1 pad AV5: (no net) -> GND
- JCPU1 pad AV9: (no net) -> GND
- JCPU1 pad AW10: (no net) -> unconnected-(JCPU1I-VDDQ-PadAW10)
- JCPU1 pad AW14: (no net) -> unconnected-(JCPU1I-VDDQ-PadAW14)
- JCPU1 pad AW2: (no net) -> unconnected-(JCPU1J-RSVD9-PadAW2)
- JCPU1 pad AW25: (no net) -> unconnected-(JCPU1I-VDDQ-PadAW25)
- JCPU1 pad AW3: (no net) -> GND
- JCPU1 pad AW30: (no net) -> GND
- JCPU1 pad AW32: (no net) -> GND
- JCPU1 pad AW34: (no net) -> GND
- JCPU1 pad AW36: (no net) -> GND
- JCPU1 pad AW38: (no net) -> GND
- JCPU1 pad AW5: (no net) -> GND
- JCPU1 pad AW9: (no net) -> GND
- JCPU1 pad AY12: (no net) -> unconnected-(JCPU1I-VDDQ-PadAY12)
- JCPU1 pad AY16: (no net) -> unconnected-(JCPU1I-VDDQ-PadAY16)
- JCPU1 pad AY18: (no net) -> unconnected-(JCPU1I-VDDQ-PadAY18)
- JCPU1 pad AY23: (no net) -> unconnected-(JCPU1I-VDDQ-PadAY23)
- JCPU1 pad AY27: (no net) -> GND
- JCPU1 pad AY3: (no net) -> GND
- JCPU1 pad AY30: (no net) -> GND
- JCPU1 pad AY5: (no net) -> GND
- JCPU1 pad AY7: (no net) -> GND
- JCPU1 pad AY9: (no net) -> GND
- JCPU1 pad B10: (no net) -> unconnected-(JCPU1E-PROC_PRDY#-PadB10)
- JCPU1 pad B11: (no net) -> unconnected-(JCPU1D-DDI3_AUXP-PadB11)
- JCPU1 pad B12: (no net) -> unconnected-(JCPU1D-DDI2_AUXN-PadB12)
- JCPU1 pad B13: (no net) -> unconnected-(JCPU1D-DDI1_AUXP-PadB13)
- JCPU1 pad B14: (no net) -> unconnected-(JCPU1D-DDI3_TXP_0-PadB14)
- JCPU1 pad B15: (no net) -> unconnected-(JCPU1D-DDI3_TXN_1-PadB15)
- JCPU1 pad B16: (no net) -> unconnected-(JCPU1D-DDI3_TXP_2-PadB16)
- JCPU1 pad B17: (no net) -> unconnected-(JCPU1D-DDI3_TXN_3-PadB17)
- JCPU1 pad B18: (no net) -> unconnected-(JCPU1D-DDI2_TXP_0-PadB18)
- JCPU1 pad B23: (no net) -> unconnected-(JCPU1D-DDI1_TXP_2-PadB23)
- JCPU1 pad B24: (no net) -> GND
- JCPU1 pad B25: (no net) -> unconnected-(JCPU1G-VCC_CORE-PadB25)
- JCPU1 pad B26: (no net) -> GND
- JCPU1 pad B27: (no net) -> unconnected-(JCPU1G-VCC_CORE-PadB27)
- JCPU1 pad B28: (no net) -> GND
- JCPU1 pad B29: (no net) -> unconnected-(JCPU1G-VCC_CORE-PadB29)
- JCPU1 pad B3: (no net) -> unconnected-(JCPU1J-PROC_TRIGOUT-PadB3)
- JCPU1 pad B30: (no net) -> GND
- JCPU1 pad B31: (no net) -> unconnected-(JCPU1G-VCC_CORE-PadB31)
- JCPU1 pad B32: (no net) -> unconnected-(JCPU1G-VCC_CORE-PadB32)
- JCPU1 pad B33: (no net) -> unconnected-(JCPU1G-VCC_CORE-PadB33)
- JCPU1 pad B34: (no net) -> unconnected-(JCPU1G-VCC_CORE-PadB34)
- JCPU1 pad B35: (no net) -> unconnected-(JCPU1G-VCC_CORE-PadB35)
- JCPU1 pad B36: (no net) -> unconnected-(JCPU1G-VCC_CORE-PadB36)
- JCPU1 pad B37: (no net) -> unconnected-(JCPU1G-VCC_CORE-PadB37)
- JCPU1 pad B38: (no net) -> GND
- JCPU1 pad B39: (no net) -> unconnected-(JCPU1J-RSVD10-PadB39)
- JCPU1 pad B4: (no net) -> unconnected-(JCPU1C-PEG_TXP_1-PadB4)
- JCPU1 pad B5: (no net) -> unconnected-(JCPU1C-PEG_TXN_1-PadB5)
- JCPU1 pad B6: (no net) -> GND
- JCPU1 pad B7: (no net) -> unconnected-(JCPU1C-PEG_RXN_0-PadB7)
- JCPU1 pad B8: (no net) -> unconnected-(JCPU1C-PEG_RXP_0-PadB8)
- JCPU1 pad B9: (no net) -> unconnected-(JCPU1E-PROC_PREQ#-PadB9)
- JCPU1 pad C10: (no net) -> GND
- JCPU1 pad C11: (no net) -> unconnected-(JCPU1D-DDI3_AUXN-PadC11)
- JCPU1 pad C12: (no net) -> GND
- JCPU1 pad C13: (no net) -> unconnected-(JCPU1D-DDI1_AUXN-PadC13)
- JCPU1 pad C14: (no net) -> GND
- JCPU1 pad C15: (no net) -> unconnected-(JCPU1D-DDI3_TXP_1-PadC15)
- JCPU1 pad C16: (no net) -> GND
- JCPU1 pad C17: (no net) -> unconnected-(JCPU1D-DDI3_TXP_3-PadC17)
- JCPU1 pad C18: (no net) -> GND
- JCPU1 pad C19: (no net) -> unconnected-(JCPU1D-DDI2_TXP_2-PadC19)
- JCPU1 pad C2: (no net) -> GND
- JCPU1 pad C20: (no net) -> GND
- JCPU1 pad C21: (no net) -> unconnected-(JCPU1D-DDI1_TXP_0-PadC21)
- JCPU1 pad C22: (no net) -> GND
- JCPU1 pad C23: (no net) -> unconnected-(JCPU1D-DDI1_TXP_3-PadC23)
- JCPU1 pad C24: (no net) -> GND
- JCPU1 pad C25: (no net) -> unconnected-(JCPU1G-VCC_CORE-PadC25)
- JCPU1 pad C26: (no net) -> unconnected-(JCPU1G-VCC_CORE-PadC26)
- JCPU1 pad C27: (no net) -> unconnected-(JCPU1G-VCC_CORE-PadC27)
- JCPU1 pad C28: (no net) -> unconnected-(JCPU1G-VCC_CORE-PadC28)
- JCPU1 pad C29: (no net) -> unconnected-(JCPU1G-VCC_CORE-PadC29)
- JCPU1 pad C3: (no net) -> unconnected-(JCPU1C-PEG_TXP_2-PadC3)
- JCPU1 pad C30: (no net) -> unconnected-(JCPU1G-VCC_CORE-PadC30)
- JCPU1 pad C31: (no net) -> GND
- JCPU1 pad C32: (no net) -> unconnected-(JCPU1G-VCC_CORE-PadC32)
- JCPU1 pad C33: (no net) -> GND
- JCPU1 pad C34: (no net) -> unconnected-(JCPU1G-VCC_CORE-PadC34)
- JCPU1 pad C35: (no net) -> GND
- JCPU1 pad C36: (no net) -> unconnected-(JCPU1G-VCC_CORE-PadC36)
- JCPU1 pad C37: (no net) -> GND
- JCPU1 pad C38: (no net) -> unconnected-(JCPU1G-VCC_SENSE-PadC38)
- JCPU1 pad C39: (no net) -> unconnected-(JCPU1E-PROCHOT#-PadC39)
- JCPU1 pad C4: (no net) -> unconnected-(JCPU1C-PEG_TXN_2-PadC4)
- JCPU1 pad C40: (no net) -> unconnected-(JCPU1J-RSVD11-PadC40)
- JCPU1 pad C5: (no net) -> GND
- JCPU1 pad C6: (no net) -> unconnected-(JCPU1C-PEG_RXN_1-PadC6)
- JCPU1 pad C7: (no net) -> unconnected-(JCPU1C-PEG_RXP_1-PadC7)
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
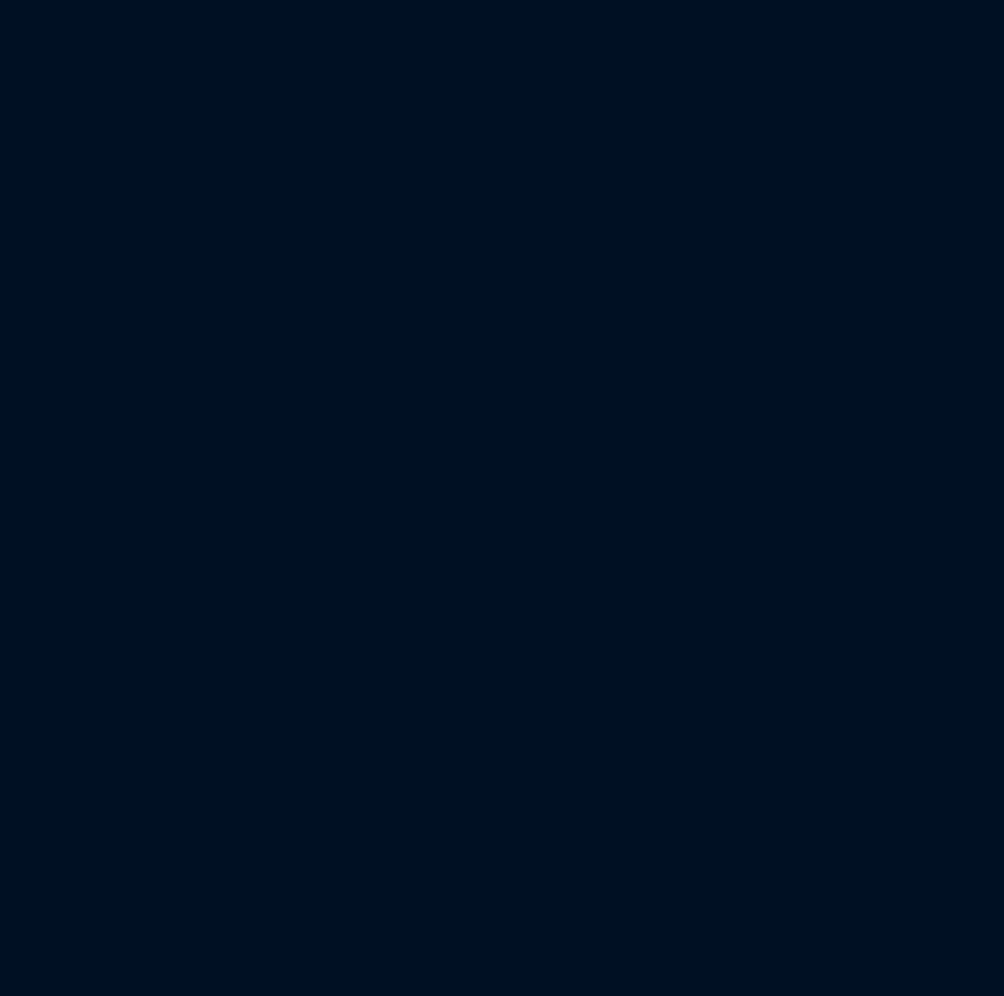
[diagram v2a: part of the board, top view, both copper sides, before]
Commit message: Added first PCH symbol and footprint
THANKS @mothenjoyer69 so much for extracting and converting the PCH footprint from a laptop boardview ❤️
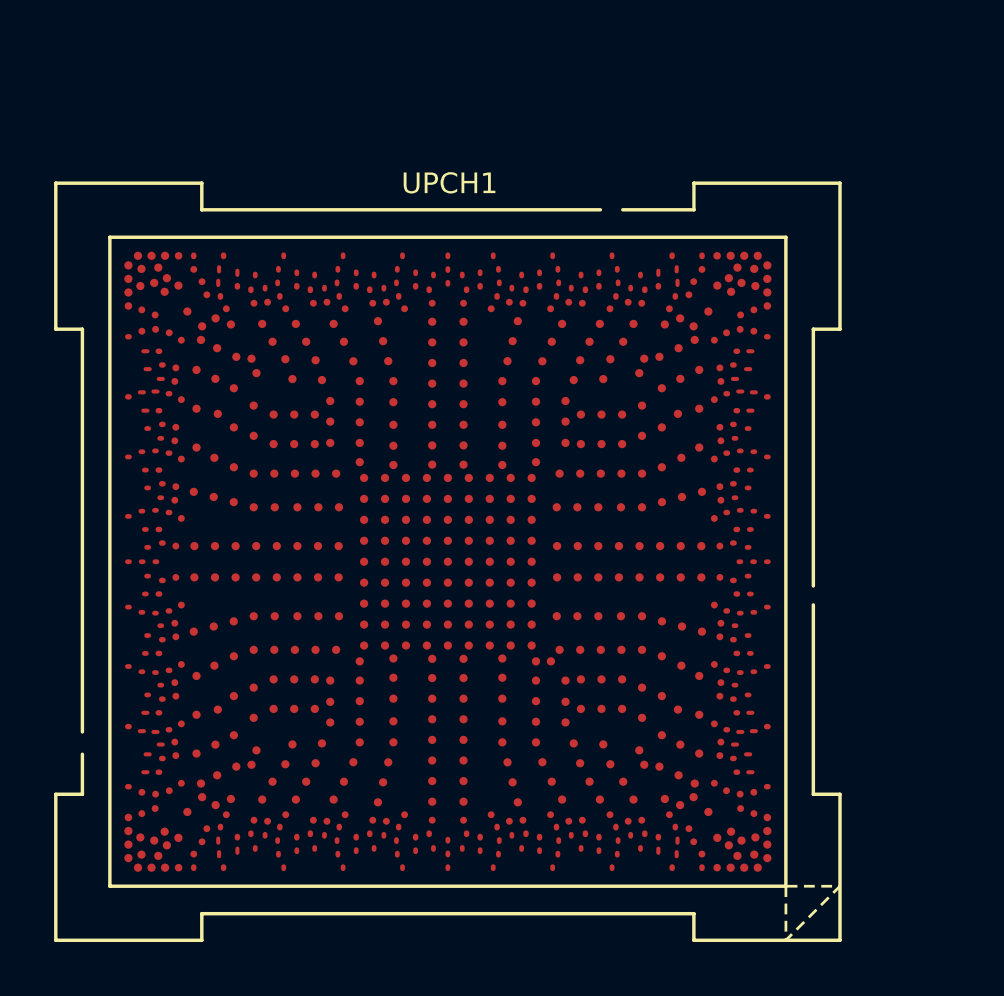
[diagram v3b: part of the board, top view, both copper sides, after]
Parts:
- added UPCH1: Intel Cannon Point 300-Series Platform Controller Hub, A-my-stuff:CNP-H_BGA_874P-T, F.Cu at (135.7, 104.7)
- JCPU1: value ~ -> Intel 8th/9th Generation Coffee-Lake LGA1151 CPU

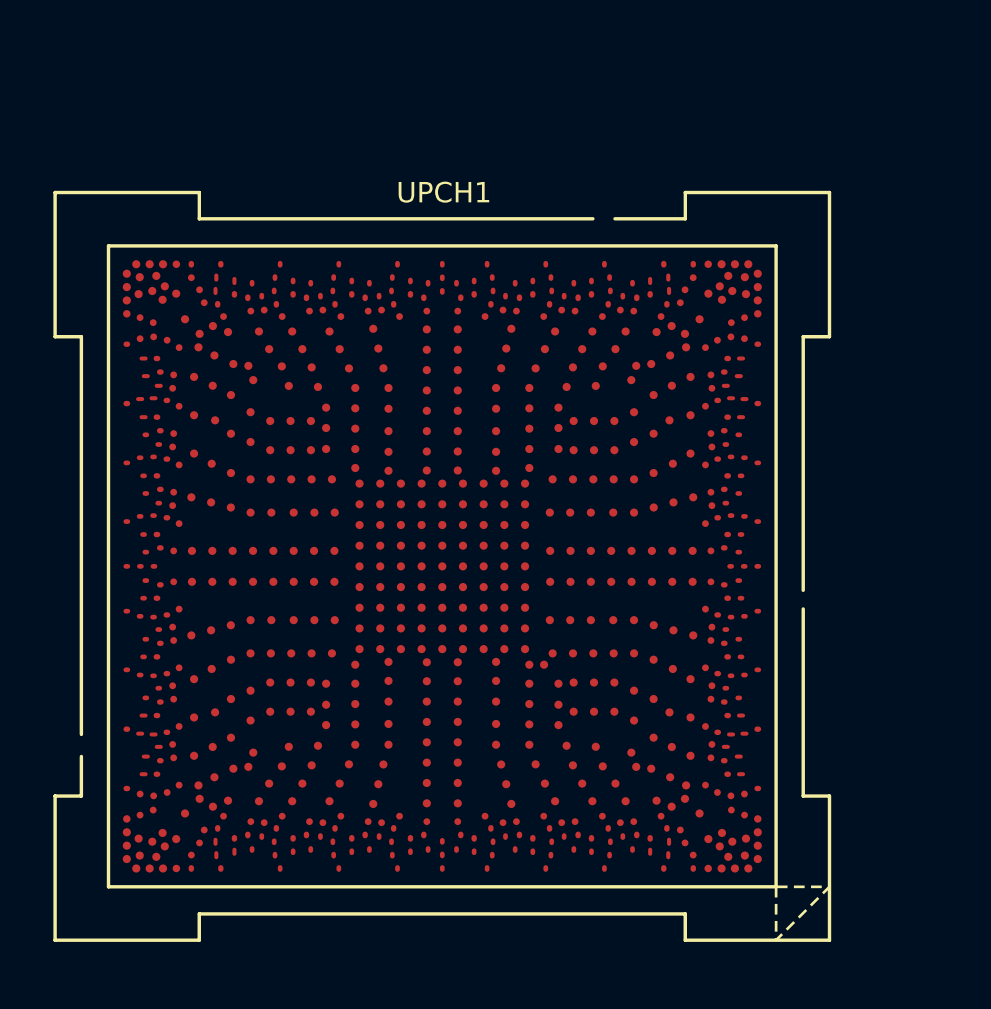
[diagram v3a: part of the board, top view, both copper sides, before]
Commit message: Added all the PCH symbols
that took 1.5 days straight lol
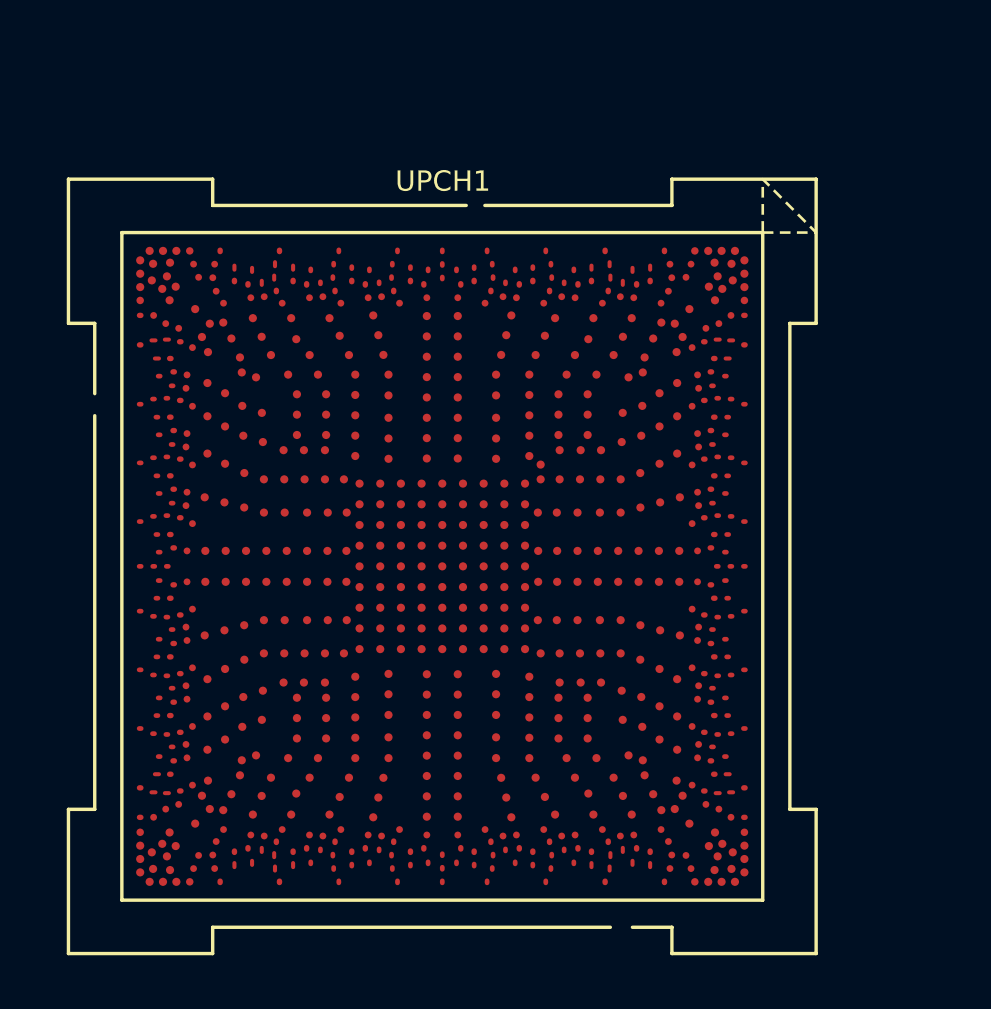
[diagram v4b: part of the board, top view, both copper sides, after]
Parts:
- turned UPCH1 to 90 degrees
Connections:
- JCPU1 pad J5: unconnected-(JCPU1C-PEG_RXP_7-PadJ5) -> (no net)
